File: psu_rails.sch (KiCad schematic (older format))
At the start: 17 parts

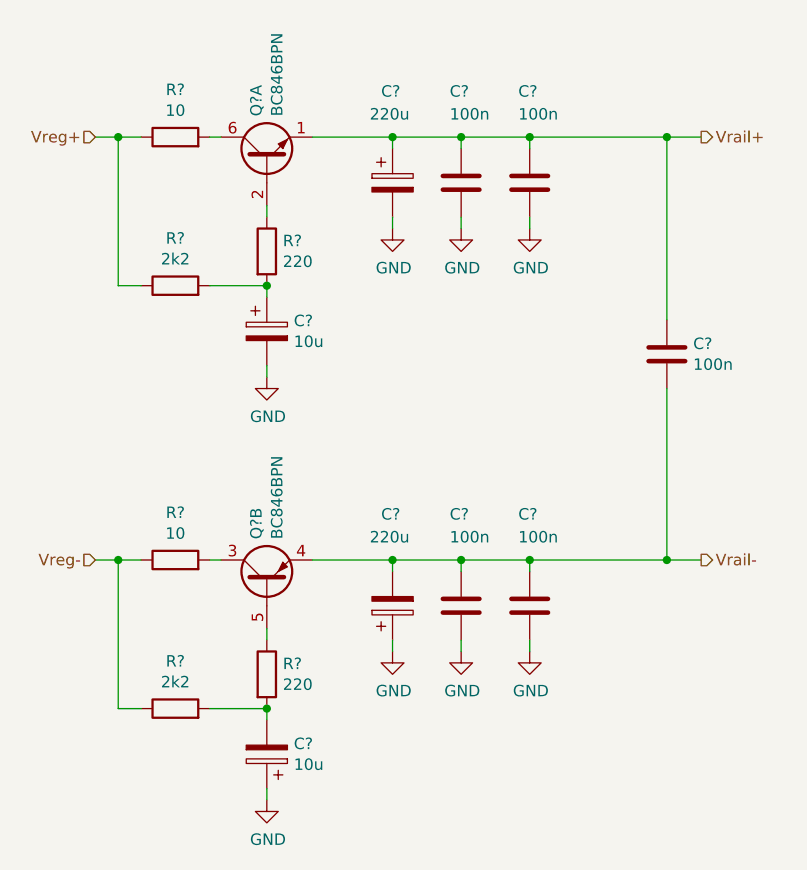
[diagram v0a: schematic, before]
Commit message: Finalise schematics with power supplies and successful ERC
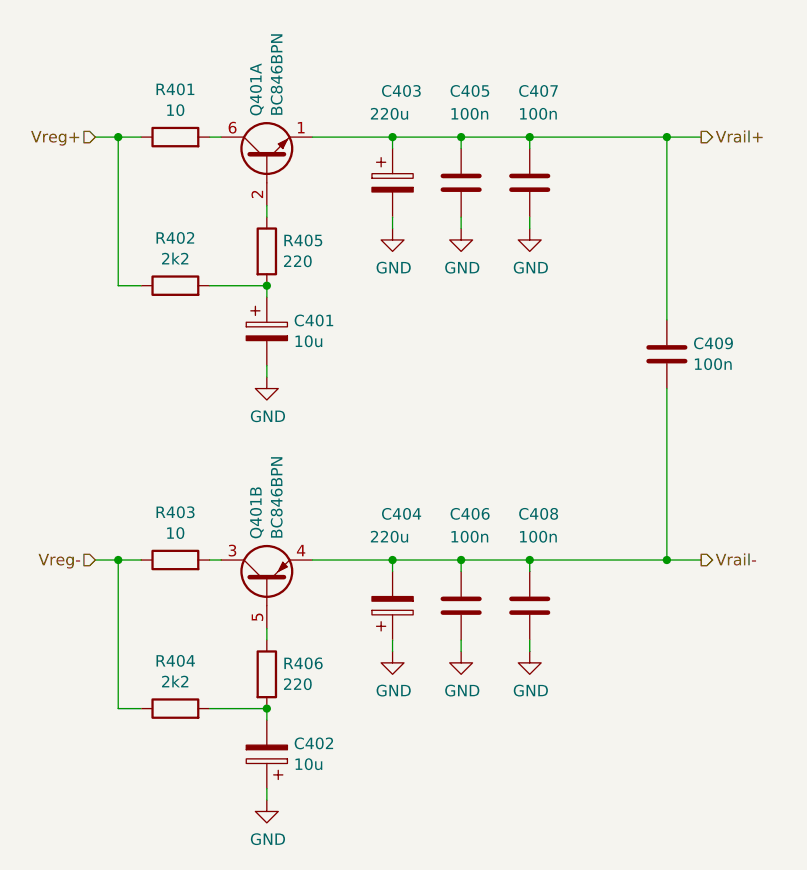
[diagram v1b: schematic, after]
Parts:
- gave numbers to parts that had none: 16
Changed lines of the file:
@@
 $EndDescr
 $Comp
-L Transistor_BJT:BC846BPN Q?
+L Transistor_BJT:BC846BPN Q401
 U 1 1 5D8DB789
 P 4500 2900
-F 0 "Q?" H 4691 2946 50  0000 L CNN
+AR Path="/5D8DB5B0/5D8DB789" Ref="Q401"  Part="1"
+AR Path="/5D8E5F02/5D8DB789" Ref="Q501"  Part="1"
+F 0 "Q401" H 4691 2946 50  0000 L CNN
 F 1 "BC846BPN" H 4691 2855 50  0000 L CNN
 F 2 "Package_TO_SOT_SMD:SOT-363_SC-70-6" H 4700 3000 50  0001 C CNN
@@
 $EndComp
 $Comp
-L Transistor_BJT:BC846BPN Q?
+L Transistor_BJT:BC846BPN Q401
 U 2 1 5D8DB7C6
 P 4500 4750
-F 0 "Q?" H 4691 4796 50  0000 L CNN
+AR Path="/5D8DB5B0/5D8DB7C6" Ref="Q401"  Part="2"
+AR Path="/5D8E5F02/5D8DB7C6" Ref="Q501"  Part="2"
+F 0 "Q401" H 4691 4796 50  0000 L CNN
 F 1 "BC846BPN" H 4691 4705 50  0000 L CNN
 F 2 "Package_TO_SOT_SMD:SOT-363_SC-70-6" H 4700 4850 50  0001 C CNN
@@
 $EndComp
 $Comp
-L Device:C C?
+L Device:C C405
 U 1 1 5D8DBC14
 P 5350 3000
-F 0 "C?" H 5300 3400 50  0000 L CNN
+AR Path="/5D8DB5B0/5D8DBC14" Ref="C405"  Part="1"
+AR Path="/5D8E5F02/5D8DBC14" Ref="C505"  Part="1"
+F 0 "C405" H 5300 3400 50  0000 L CNN
 F 1 "100n" H 5300 3300 50  0000 L CNN
 F 2 "" H 5388 2850 50  0001 C CNN
@@
 $EndComp
 $Comp
-L Device:C C?
+L Device:C C407
 U 1 1 5D8DBC36
 P 5650 3000
-F 0 "C?" H 5600 3400 50  0000 L CNN
+AR Path="/5D8DB5B0/5D8DBC36" Ref="C407"  Part="1"
+AR Path="/5D8E5F02/5D8DBC36" Ref="C507"  Part="1"
+F 0 "C407" H 5600 3400 50  0000 L CNN
 F 1 "100n" H 5600 3300 50  0000 L CNN
 F 2 "" H 5688 2850 50  0001 C CNN
@@
 $EndComp
 $Comp
-L Device:CP C?
+L Device:CP C403
 U 1 1 5D8DBD04
 P 5050 3000
-F 0 "C?" H 5000 3400 50  0000 L CNN
+AR Path="/5D8DB5B0/5D8DBD04" Ref="C403"  Part="1"
+AR Path="/5D8E5F02/5D8DBD04" Ref="C503"  Part="1"
+F 0 "C403" H 5000 3400 50  0000 L CNN
 F 1 "220u" H 4950 3300 50  0000 L CNN
 F 2 "" H 5088 2850 50  0001 C CNN
@@
 	5050 2800 5350 2800
 $Comp
-L power:GND #PWR?
+L power:GND #PWR0403
 U 1 1 5D8DBE1B
 P 5050 3200
-F 0 "#PWR?" H 5050 2950 50  0001 C CNN
+AR Path="/5D8DB5B0/5D8DBE1B" Ref="#PWR0403"  Part="1"
+AR Path="/5D8E5F02/5D8DBE1B" Ref="#PWR0503"  Part="1"
+F 0 "#PWR0503" H 5050 2950 50  0001 C CNN
 F 1 "GND" H 5055 3027 50  0000 C CNN
 F 2 "" H 5050 3200 50  0001 C CNN
@@
 $EndComp
 $Comp
-L power:GND #PWR?
+L power:GND #PWR0405
 U 1 1 5D8DBE37
 P 5350 3200
-F 0 "#PWR?" H 5350 2950 50  0001 C CNN
+AR Path="/5D8DB5B0/5D8DBE37" Ref="#PWR0405"  Part="1"
+AR Path="/5D8E5F02/5D8DBE37" Ref="#PWR0505"  Part="1"
+F 0 "#PWR0505" H 5350 2950 50  0001 C CNN
 F 1 "GND" H 5355 3027 50  0000 C CNN
 F 2 "" H 5350 3200 50  0001 C CNN
@@
 $EndComp
 $Comp
-L power:GND #PWR?
+L power:GND #PWR0407
 U 1 1 5D8DBE4C
 P 5650 3200
-F 0 "#PWR?" H 5650 2950 50  0001 C CNN
+AR Path="/5D8DB5B0/5D8DBE4C" Ref="#PWR0407"  Part="1"
+AR Path="/5D8E5F02/5D8DBE4C" Ref="#PWR0507"  Part="1"
+F 0 "#PWR0507" H 5650 2950 50  0001 C CNN
 F 1 "GND" H 5655 3027 50  0000 C CNN
 F 2 "" H 5650 3200 50  0001 C CNN
@@
 	5050 4650 5350 4650
 $Comp
-L power:GND #PWR?
+L power:GND #PWR0404
 U 1 1 5D8DBF9B
 P 5050 5050
-F 0 "#PWR?" H 5050 4800 50  0001 C CNN
+AR Path="/5D8DB5B0/5D8DBF9B" Ref="#PWR0404"  Part="1"
+AR Path="/5D8E5F02/5D8DBF9B" Ref="#PWR0504"  Part="1"
+F 0 "#PWR0504" H 5050 4800 50  0001 C CNN
 F 1 "GND" H 5055 4877 50  0000 C CNN
 F 2 "" H 5050 5050 50  0001 C CNN
@@
 $EndComp
 $Comp
-L power:GND #PWR?
+L power:GND #PWR0406
 U 1 1 5D8DBFA1
 P 5350 5050
-F 0 "#PWR?" H 5350 4800 50  0001 C CNN
+AR Path="/5D8DB5B0/5D8DBFA1" Ref="#PWR0406"  Part="1"
+AR Path="/5D8E5F02/5D8DBFA1" Ref="#PWR0506"  Part="1"
+F 0 "#PWR0506" H 5350 4800 50  0001 C CNN
 F 1 "GND" H 5355 4877 50  0000 C CNN
 F 2 "" H 5350 5050 50  0001 C CNN
@@
 $EndComp
 $Comp
-L power:GND #PWR?
+L power:GND #PWR0408
 U 1 1 5D8DBFA7
 P 5650 5050
-F 0 "#PWR?" H 5650 4800 50  0001 C CNN
+AR Path="/5D8DB5B0/5D8DBFA7" Ref="#PWR0408"  Part="1"
+AR Path="/5D8E5F02/5D8DBFA7" Ref="#PWR0508"  Part="1"
+F 0 "#PWR0508" H 5650 4800 50  0001 C CNN
 F 1 "GND" H 5655 4877 50  0000 C CNN
 F 2 "" H 5650 5050 50  0001 C CNN
@@
 	5650 5050 5650 5000
 $Comp
-L Device:C C?
+L Device:C C409
 U 1 1 5D8DC249
 P 6250 3750
-F 0 "C?" H 6365 3796 50  0000 L CNN
+AR Path="/5D8DB5B0/5D8DC249" Ref="C409"  Part="1"
+AR Path="/5D8E5F02/5D8DC249" Ref="C509"  Part="1"
+F 0 "C409" H 6365 3796 50  0000 L CNN
 F 1 "100n" H 6365 3705 50  0000 L CNN
 F 2 "" H 6288 3600 50  0001 C CNN
@@
 Connection ~ 5650 4650
 $Comp
-L Device:C C?
+L Device:C C406
 U 1 1 5D8DCC24
 P 5350 4850
-F 0 "C?" H 5300 5250 50  0000 L CNN
+AR Path="/5D8DB5B0/5D8DCC24" Ref="C406"  Part="1"
+AR Path="/5D8E5F02/5D8DCC24" Ref="C506"  Part="1"
+F 0 "C406" H 5300 5250 50  0000 L CNN
 F 1 "100n" H 5300 5150 50  0000 L CNN
 F 2 "" H 5388 4700 50  0001 C CNN
@@
 $EndComp
 $Comp
-L Device:C C?
+L Device:C C408
 U 1 1 5D8DCC2A
 P 5650 4850
-F 0 "C?" H 5600 5250 50  0000 L CNN
+AR Path="/5D8DB5B0/5D8DCC2A" Ref="C408"  Part="1"
+AR Path="/5D8E5F02/5D8DCC2A" Ref="C508"  Part="1"
+F 0 "C408" H 5600 5250 50  0000 L CNN
 F 1 "100n" H 5600 5150 50  0000 L CNN
 F 2 "" H 5688 4700 50  0001 C CNN
@@
 $EndComp
 $Comp
-L Device:CP C?
+L Device:CP C404
 U 1 1 5D8DCC30
 P 5050 4850
-F 0 "C?" H 5000 4450 50  0000 L CNN
+AR Path="/5D8DB5B0/5D8DCC30" Ref="C404"  Part="1"
+AR Path="/5D8E5F02/5D8DCC30" Ref="C504"  Part="1"
+F 0 "C404" H 5000 4450 50  0000 L CNN
 F 1 "220u" H 4950 4550 50  0000 L CNN
 F 2 "" H 5088 4700 50  0001 C CNN
@@
 $EndComp
 $Comp
-L Device:CP C?
+L Device:CP C401
 U 1 1 5D8DDC3C
 P 4500 3650
-F 0 "C?" H 4618 3696 50  0000 L CNN
+AR Path="/5D8DB5B0/5D8DDC3C" Ref="C401"  Part="1"
+AR Path="/5D8E5F02/5D8DDC3C" Ref="C501"  Part="1"
+F 0 "C401" H 4618 3696 50  0000 L CNN
 F 1 "10u" H 4618 3605 50  0000 L CNN
 F 2 "" H 4538 3500 50  0001 C CNN
@@
 $EndComp
 $Comp
-L Device:CP C?
+L Device:CP C402
 U 1 1 5D8DE233
 P 4500 5500
-F 0 "C?" H 4382 5454 50  0000 R CNN
+AR Path="/5D8DB5B0/5D8DE233" Ref="C402"  Part="1"
+AR Path="/5D8E5F02/5D8DE233" Ref="C502"  Part="1"
+F 0 "C402" H 4382 5454 50  0000 R CNN
 F 1 "10u" H 4382 5545 50  0000 R CNN
 F 2 "" H 4538 5350 50  0001 C CNN
@@
 	4500 3150 4500 3100
 $Comp
-L Device:R R?
+L Device:R R405
 U 1 1 5D8DF470
 P 4500 3300
-F 0 "R?" H 4570 3346 50  0000 L CNN
+AR Path="/5D8DB5B0/5D8DF470" Ref="R405"  Part="1"
+AR Path="/5D8E5F02/5D8DF470" Ref="R505"  Part="1"
+F 0 "R405" H 4570 3346 50  0000 L CNN
 F 1 "220" H 4570 3255 50  0000 L CNN
 F 2 "" V 4430 3300 50  0001 C CNN
@@
 $EndComp
 $Comp
-L Device:R R?
+L Device:R R406
 U 1 1 5D8DF4B2
 P 4500 5150
-F 0 "R?" H 4570 5196 50  0000 L CNN
+AR Path="/5D8DB5B0/5D8DF4B2" Ref="R406"  Part="1"
+AR Path="/5D8E5F02/5D8DF4B2" Ref="R506"  Part="1"
+F 0 "R406" H 4570 5196 50  0000 L CNN
 F 1 "220" H 4570 5105 50  0000 L CNN
 F 2 "" V 4430 5150 50  0001 C CNN
@@
 $EndComp
 $Comp
-L power:GND #PWR?
+L power:GND #PWR0401
 U 1 1 5D8DF531
 P 4500 3850
-F 0 "#PWR?" H 4500 3600 50  0001 C CNN
+AR Path="/5D8DB5B0/5D8DF531" Ref="#PWR0401"  Part="1"
+AR Path="/5D8E5F02/5D8DF531" Ref="#PWR0501"  Part="1"
+F 0 "#PWR0501" H 4500 3600 50  0001 C CNN
 F 1 "GND" H 4505 3677 50  0000 C CNN
 F 2 "" H 4500 3850 50  0001 C CNN
@@
 $EndComp
 $Comp
-L power:GND #PWR?
+L power:GND #PWR0402
 U 1 1 5D8DF556
 P 4500 5700
-F 0 "#PWR?" H 4500 5450 50  0001 C CNN
+AR Path="/5D8DB5B0/5D8DF556" Ref="#PWR0402"  Part="1"
+AR Path="/5D8E5F02/5D8DF556" Ref="#PWR0502"  Part="1"
+F 0 "#PWR0502" H 4500 5450 50  0001 C CNN
 F 1 "GND" H 4505 5527 50  0000 C CNN
 F 2 "" H 4500 5700 50  0001 C CNN
@@
 Connection ~ 6250 4650
 $Comp
-L Device:R R?
+L Device:R R401
 U 1 1 5D8E16D4
 P 4100 2800
-F 0 "R?" V 4307 2800 50  0000 C CNN
+AR Path="/5D8DB5B0/5D8E16D4" Ref="R401"  Part="1"
+AR Path="/5D8E5F02/5D8E16D4" Ref="R501"  Part="1"
+F 0 "R401" V 4307 2800 50  0000 C CNN
 F 1 "10" V 4216 2800 50  0000 C CNN
 F 2 "" V 4030 2800 50  0001 C CNN
@@
 $EndComp
 $Comp
-L Device:R R?
+L Device:R R402
 U 1 1 5D8E1F53
 P 4100 3450
-F 0 "R?" V 4307 3450 50  0000 C CNN
+AR Path="/5D8DB5B0/5D8E1F53" Ref="R402"  Part="1"
+AR Path="/5D8E5F02/5D8E1F53" Ref="R502"  Part="1"
+F 0 "R402" V 4307 3450 50  0000 C CNN
 F 1 "2k2" V 4216 3450 50  0000 C CNN
 F 2 "" V 4030 3450 50  0001 C CNN
@@
 $EndComp
 $Comp
-L Device:R R?
+L Device:R R403
 U 1 1 5D8E1F97
 P 4100 4650
-F 0 "R?" V 4307 4650 50  0000 C CNN
+AR Path="/5D8DB5B0/5D8E1F97" Ref="R403"  Part="1"
+AR Path="/5D8E5F02/5D8E1F97" Ref="R503"  Part="1"
+F 0 "R403" V 4307 4650 50  0000 C CNN
 F 1 "10" V 4216 4650 50  0000 C CNN
 F 2 "" V 4030 4650 50  0001 C CNN
@@
 $EndComp
 $Comp
-L Device:R R?
+L Device:R R404
 U 1 1 5D8E1FEF
 P 4100 5300
-F 0 "R?" V 4307 5300 50  0000 C CNN
+AR Path="/5D8DB5B0/5D8E1FEF" Ref="R404"  Part="1"
+AR Path="/5D8E5F02/5D8E1FEF" Ref="R504"  Part="1"
+F 0 "R404" V 4307 5300 50  0000 C CNN
 F 1 "2k2" V 4216 5300 50  0000 C CNN
 F 2 "" V 4030 5300 50  0001 C CNN

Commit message: Finalise BOM
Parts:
- C401, C402: symbol Device:CP -> Device:C; Parameters (none) -> X7R/X5R 25V 1206; Part number (none) -> C1206C106K3PACTU
- C403, C404: Parameters (none) -> SMT Electrolytic 25V; Part number (none) -> EEE1HA221UAP
- C405, C406, C407, C408, C409: Parameters (none) -> X7R/X5R 0603; Part number (none) -> VJ0603Y104KXACW1BC
- Q401: Part number (none) -> BC846BPN
- R401, R403: value 10 -> 10 1/8W; Parameters (none) -> Thin Film 0805; Part number (none) -> MCWF08U10RBTL
- R402, R404: Parameters (none) -> Thin Film 0603; Part number (none) -> RT0603FRE072K2L
- R405, R406: Parameters (none) -> Thin Film 0603; Part number (none) -> ERA3AEB221V
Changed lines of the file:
@@
 F 2 "Package_TO_SOT_SMD:SOT-363_SC-70-6" H 4700 3000 50  0001 C CNN
 F 3 "https://assets.nexperia.com/documents/data-sheet/BC846BPN.pdf" H 4500 2900 50  0001 C CNN
+F 4 "BC846BPN" H 0   0   50  0001 C CNN "Part number"
 	1    4500 2900
 	0    -1   -1   0
@@
 F 2 "Package_TO_SOT_SMD:SOT-363_SC-70-6" H 4700 4850 50  0001 C CNN
 F 3 "https://assets.nexperia.com/documents/data-sheet/BC846BPN.pdf" H 4500 4750 50  0001 C CNN
+F 4 "BC846BPN" H 0   0   50  0001 C CNN "Part number"
 	2    4500 4750
 	0    -1   -1   0
@@
 F 2 "" H 5388 2850 50  0001 C CNN
 F 3 "~" H 5350 3000 50  0001 C CNN
+F 4 "VJ0603Y104KXACW1BC" H 0   0   50  0001 C CNN "Part number"
+F 5 "X7R/X5R 0603" H 0   0   50  0001 C CNN "Parameters"
 	1    5350 3000
 	1    0    0    -1
@@
 F 2 "" H 5688 2850 50  0001 C CNN
 F 3 "~" H 5650 3000 50  0001 C CNN
+F 4 "VJ0603Y104KXACW1BC" H 0   0   50  0001 C CNN "Part number"
+F 5 "X7R/X5R 0603" H 0   0   50  0001 C CNN "Parameters"
 	1    5650 3000
 	1    0    0    -1
@@
 F 2 "" H 5088 2850 50  0001 C CNN
 F 3 "~" H 5050 3000 50  0001 C CNN
+F 4 "EEE1HA221UAP" H 0   0   50  0001 C CNN "Part number"
+F 5 "SMT Electrolytic 25V" H 0   0   50  0001 C CNN "Parameters"
 	1    5050 3000
 	1    0    0    -1
@@
 AR Path="/5D8DB5B0/5D8DBE1B" Ref="#PWR0403"  Part="1"
 AR Path="/5D8E5F02/5D8DBE1B" Ref="#PWR0503"  Part="1"
-F 0 "#PWR0503" H 5050 2950 50  0001 C CNN
+F 0 "#PWR0403" H 5050 2950 50  0001 C CNN
 F 1 "GND" H 5055 3027 50  0000 C CNN
 F 2 "" H 5050 3200 50  0001 C CNN
@@
 AR Path="/5D8DB5B0/5D8DBE37" Ref="#PWR0405"  Part="1"
 AR Path="/5D8E5F02/5D8DBE37" Ref="#PWR0505"  Part="1"
-F 0 "#PWR0505" H 5350 2950 50  0001 C CNN
+F 0 "#PWR0405" H 5350 2950 50  0001 C CNN
 F 1 "GND" H 5355 3027 50  0000 C CNN
 F 2 "" H 5350 3200 50  0001 C CNN
@@
 AR Path="/5D8DB5B0/5D8DBE4C" Ref="#PWR0407"  Part="1"
 AR Path="/5D8E5F02/5D8DBE4C" Ref="#PWR0507"  Part="1"
-F 0 "#PWR0507" H 5650 2950 50  0001 C CNN
+F 0 "#PWR0407" H 5650 2950 50  0001 C CNN
 F 1 "GND" H 5655 3027 50  0000 C CNN
 F 2 "" H 5650 3200 50  0001 C CNN
@@
 AR Path="/5D8DB5B0/5D8DBF9B" Ref="#PWR0404"  Part="1"
 AR Path="/5D8E5F02/5D8DBF9B" Ref="#PWR0504"  Part="1"
-F 0 "#PWR0504" H 5050 4800 50  0001 C CNN
+F 0 "#PWR0404" H 5050 4800 50  0001 C CNN
 F 1 "GND" H 5055 4877 50  0000 C CNN
 F 2 "" H 5050 5050 50  0001 C CNN
@@
 AR Path="/5D8DB5B0/5D8DBFA1" Ref="#PWR0406"  Part="1"
 AR Path="/5D8E5F02/5D8DBFA1" Ref="#PWR0506"  Part="1"
-F 0 "#PWR0506" H 5350 4800 50  0001 C CNN
+F 0 "#PWR0406" H 5350 4800 50  0001 C CNN
 F 1 "GND" H 5355 4877 50  0000 C CNN
 F 2 "" H 5350 5050 50  0001 C CNN
@@
 AR Path="/5D8DB5B0/5D8DBFA7" Ref="#PWR0408"  Part="1"
 AR Path="/5D8E5F02/5D8DBFA7" Ref="#PWR0508"  Part="1"
-F 0 "#PWR0508" H 5650 4800 50  0001 C CNN
+F 0 "#PWR0408" H 5650 4800 50  0001 C CNN
 F 1 "GND" H 5655 4877 50  0000 C CNN
 F 2 "" H 5650 5050 50  0001 C CNN
@@
 F 2 "" H 6288 3600 50  0001 C CNN
 F 3 "~" H 6250 3750 50  0001 C CNN
+F 4 "VJ0603Y104KXACW1BC" H 0   0   50  0001 C CNN "Part number"
+F 5 "X7R/X5R 0603" H 0   0   50  0001 C CNN "Parameters"
 	1    6250 3750
 	1    0    0    -1
@@
 F 2 "" H 5388 4700 50  0001 C CNN
 F 3 "~" H 5350 4850 50  0001 C CNN
+F 4 "VJ0603Y104KXACW1BC" H 0   0   50  0001 C CNN "Part number"
+F 5 "X7R/X5R 0603" H 0   0   50  0001 C CNN "Parameters"
 	1    5350 4850
 	1    0    0    -1
@@
 F 2 "" H 5688 4700 50  0001 C CNN
 F 3 "~" H 5650 4850 50  0001 C CNN
+F 4 "VJ0603Y104KXACW1BC" H 0   0   50  0001 C CNN "Part number"
+F 5 "X7R/X5R 0603" H 0   0   50  0001 C CNN "Parameters"
 	1    5650 4850
 	1    0    0    -1
@@
 F 2 "" H 5088 4700 50  0001 C CNN
 F 3 "~" H 5050 4850 50  0001 C CNN
+F 4 "EEE1HA221UAP" H 0   0   50  0001 C CNN "Part number"
+F 5 "SMT Electrolytic 25V" H 0   0   50  0001 C CNN "Parameters"
 	1    5050 4850
 	1    0    0    1
 $EndComp
 $Comp
-L Device:CP C401
+L Device:C C401
 U 1 1 5D8DDC3C
 P 4500 3650
@@
 F 2 "" H 4538 3500 50  0001 C CNN
 F 3 "~" H 4500 3650 50  0001 C CNN
+F 4 "X7R/X5R 25V 1206" H 0   0   50  0001 C CNN "Parameters"
+F 5 "C1206C106K3PACTU" H 0   0   50  0001 C CNN "Part number"
 	1    4500 3650
 	1    0    0    -1
 $EndComp
 $Comp
-L Device:CP C402
+L Device:C C402
 U 1 1 5D8DE233
 P 4500 5500
@@
 F 2 "" H 4538 5350 50  0001 C CNN
 F 3 "~" H 4500 5500 50  0001 C CNN
+F 4 "X7R/X5R 25V 1206" H 0   0   50  0001 C CNN "Parameters"
+F 5 "C1206C106K3PACTU" H 0   0   50  0001 C CNN "Part number"
 	1    4500 5500
 	-1   0    0    1
@@
 F 2 "" V 4430 3300 50  0001 C CNN
 F 3 "~" H 4500 3300 50  0001 C CNN
+F 4 "ERA3AEB221V" H 0   0   50  0001 C CNN "Part number"
+F 5 "Thin Film 0603" H 0   0   50  0001 C CNN "Parameters"
 	1    4500 3300
 	1    0    0    -1
@@
 F 2 "" V 4430 5150 50  0001 C CNN
 F 3 "~" H 4500 5150 50  0001 C CNN
+F 4 "ERA3AEB221V" H 0   0   50  0001 C CNN "Part number"
+F 5 "Thin Film 0603" H 0   0   50  0001 C CNN "Parameters"
 	1    4500 5150
 	1    0    0    -1
@@
 AR Path="/5D8DB5B0/5D8DF531" Ref="#PWR0401"  Part="1"
 AR Path="/5D8E5F02/5D8DF531" Ref="#PWR0501"  Part="1"
-F 0 "#PWR0501" H 4500 3600 50  0001 C CNN
+F 0 "#PWR0401" H 4500 3600 50  0001 C CNN
 F 1 "GND" H 4505 3677 50  0000 C CNN
 F 2 "" H 4500 3850 50  0001 C CNN
@@
 AR Path="/5D8DB5B0/5D8DF556" Ref="#PWR0402"  Part="1"
 AR Path="/5D8E5F02/5D8DF556" Ref="#PWR0502"  Part="1"
-F 0 "#PWR0502" H 4500 5450 50  0001 C CNN
+F 0 "#PWR0402" H 4500 5450 50  0001 C CNN
 F 1 "GND" H 4505 5527 50  0000 C CNN
 F 2 "" H 4500 5700 50  0001 C CNN
@@
 AR Path="/5D8E5F02/5D8E16D4" Ref="R501"  Part="1"
 F 0 "R401" V 4307 2800 50  0000 C CNN
-F 1 "10" V 4216 2800 50  0000 C CNN
+F 1 "10 1/8W" V 4216 2800 50  0000 C CNN
 F 2 "" V 4030 2800 50  0001 C CNN
 F 3 "~" H 4100 2800 50  0001 C CNN
+F 4 "MCWF08U10RBTL" H 0   0   50  0001 C CNN "Part number"
+F 5 "Thin Film 0805" H 0   0   50  0001 C CNN "Parameters"
 	1    4100 2800
 	0    -1   -1   0
@@
 F 2 "" V 4030 3450 50  0001 C CNN
 F 3 "~" H 4100 3450 50  0001 C CNN
+F 4 "RT0603FRE072K2L" H 0   0   50  0001 C CNN "Part number"
+F 5 "Thin Film 0603" H 0   0   50  0001 C CNN "Parameters"
 	1    4100 3450
 	0    -1   -1   0
@@
 AR Path="/5D8E5F02/5D8E1F97" Ref="R503"  Part="1"
 F 0 "R403" V 4307 4650 50  0000 C CNN
-F 1 "10" V 4216 4650 50  0000 C CNN
+F 1 "10 1/8W" V 4216 4650 50  0000 C CNN
 F 2 "" V 4030 4650 50  0001 C CNN
 F 3 "~" H 4100 4650 50  0001 C CNN
+F 4 "MCWF08U10RBTL" H 0   0   50  0001 C CNN "Part number"
+F 5 "Thin Film 0805" H 0   0   50  0001 C CNN "Parameters"
 	1    4100 4650
 	0    -1   -1   0
@@
 F 2 "" V 4030 5300 50  0001 C CNN
 F 3 "~" H 4100 5300 50  0001 C CNN
+F 4 "RT0603FRE072K2L" H 0   0   50  0001 C CNN "Part number"
+F 5 "Thin Film 0603" H 0   0   50  0001 C CNN "Parameters"
 	1    4100 5300
 	0    -1   -1   0
